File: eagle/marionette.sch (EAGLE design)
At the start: 483 parts, among them J12 IDC_RECEPTACLE_20PIN-S9172-ND, J13 CONN_HEADER_JTAG, J2 SP3T Jumper Switch, J22 ZX62D-B-5P8, J3 IDC_RECEPTACLE_2X20-S9175-ND, J5 CON_COAX_PWR_PJ-047AH-NO_MILL, J8 IDC_RECEPTACLE_2X20-S9175-ND, J9 IDC_RECEPTACLE_2X20-S9175-ND, M5002 IRFR9024NTRPBF, Q2 NFET_DUAL_DMN63D8LDW, Q3 AO3419, SW1 SW-MOM-TACTILE-B3F-1000, SW2 SW-MOM-TACTILE-B3F-1000, U1 SWITCH_74HC4066D, U10 LMV344, U11 STM32F427-STM32F427, U13 CON_HIROSE_DM3D(MICROSD), U14 USB3320, U15 SWITCH_74HC4066D, U17 LM3671, U2 FR014H5JZ, U3 MIC5305_MIC5305-3.3YD5, U4 DAC124S085CIMM, U40 MIC5305_MIC5305-3.3YD5, U41 MIC5305-MIC5305-1.8YD5, U5 MAX3051ESAESA+, U5002 TPS40200, U6 OPAMP_DUAL_MC4558CDT, U7 LMV344, U8 LMV344, U9 LMV344, X1 ABSO7

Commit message: marionette.sch incorporates Gavin's SPI4 and SPI6, I2C1/3 and GPIO rerouting, as well as the TPS63060 is in the schematic.  The schematic passes ERC.  The documentation for the TPS63060 on the board is in an ipython notebookgit add Datasheets/ Design/TPS63060_calculations.ipynb Design/ipython_files/ eagle/marionette.sch eagle/marionette.pdf eagle/marionette.lbr !
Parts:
- removed C112, C113, C114: 10u, rcl_custom:C-EUC1210
- removed C115, C144: 100p, rcl_custom:C-EU0402-B
- removed C116: 2.2n, rcl_custom:C-EU0402-B
- removed C117: np, rcl_custom:C-EU0402-B
- removed C147: 4.7u, rcl_custom:C-EU0805-B
- removed C155, C156: 100n, rcl_custom:C-EU0402-B
- removed D4: B130LB, marionette:DIODE_SCHOTTKY-_B130LB
- removed LED1, LED2, LED3, LED4, LED5, LED6: LS_Q976, LS_Q976_NR_1:LS_Q976
- removed M5002: IRFR9024NTRPBF, marionette:PFET-IRFR9024NTRPBF
- removed R22, R23, R24, R25, R26, R27: 620, rcl_custom:R-US_0402-B
- removed R5701: .050, rcl_custom:R_SENSE2512-6PAD_KELVIN_CONNECTION
- removed R69: 1.6k, rcl_custom:R-US_0402-B
- removed R71: 240k, rcl_custom:R-US_0402-B
- removed R96: 90.9k, rcl_custom:R-US_0402-B
- removed R97: 15k, rcl_custom:R-US_0402-B
- removed R98: 100k, rcl_custom:R-US_0402-B
- removed TP114, TP115, TP116, TP117, TP118, TP119, TP130, TP132: (no value), marionette:PAD+X-0.7-NO_CREAM+SILK
- removed TP201, TP61: PAD+VIA_0.6MM, marionette:PAD+VIA_0.6MM
- removed TP80: (no value), marionette:PAD+X-1.0-NO_CREAM+SILK
- removed U5002: TPS40200, marionette:TPS40200-SOIC-8_296-23923-6-ND
- added LED8: LS_Q976, LS_Q976_NR_1:LS_Q976
- added Q1: NX3020NAK, dock_v2:NFET-SOT23_NX3020NAK
- added R1, R4: 10k, rcl_custom:R-US_0402-B
- added R2: 1Meg, rcl_custom:R-US_0402-B
- added R3: 111k, rcl_custom:R-US_0402-B
- added TP29: PAD+VIA_0.25MM, dock_v2:PAD+VIA_0.25MM
- added TP74: PAD+VIA_0.635MM, dock_v2:PAD+VIA_0.635MM
- added U12: TPS63060, marionette:TPS63060
- C100, C104: value 100n -> 4.7u; device rcl_custom:C-EU0402-B -> rcl_custom:C-EUC1210; V_RATING 35V -> 25V
- C101: value 10u -> 10p; device rcl_custom:C-EUC1210 -> rcl_custom:C-EU0402-B; V_RATING 35V -> 10V
- C102: value 10u -> 100n; device rcl_custom:C-EUC1210 -> rcl_custom:C-EU0402-B; V_RATING 35V -> 25V
- C103: value 10u -> np; device rcl_custom:C-EUC1210 -> rcl_custom:C-EU1206-B; V_RATING 35V -> (none)
- C105, C106: value 10uF -> np; device rcl_custom:C-EUC1210 -> rcl_custom:C-EU1206-B; V_RATING 35V -> (none)
- C107, C108: value 10uF -> 4.7u; V_RATING 35V -> 25V
- C109: value 100n -> np; device rcl_custom:C-EU0402-B -> rcl_custom:C-EU1206-B; V_RATING 25V -> (none)
- C110: value 1n -> np; device rcl_custom:C-EU0402-B -> rcl_custom:C-EU1206-B; V_RATING 25V -> (none)
- C111: V_RATING 10V -> 25V
- C99: value 10u -> 100n; device rcl_custom:C-EUC1210 -> rcl_custom:C-EU0402-B
- L1: value SRF1260-4R7Y -> SRN3015-1R0 1uH; device marionette:INDUCTOR_COUPLED_SRF1260-4R7Y -> dock_v2:INDUCTOR_FERRITE_CORE_SRN3015-1R0
- R38: value 200k -> 10k
- R68: value 1k -> 3.3k
- TP32: value PAD+VIA_0.25MM -> (none); device marionette:PAD+VIA_0.25MM -> dock_v2:PAD+X-1.0-NO_CREAM+SILK
- TP45: value PAD+VIA_0.6MM -> (none); device marionette:PAD+VIA_0.6MM -> dock_v2:PAD+X-2.0-NOCREAM+SILK
- TP76: device marionette:PAD+X-0.7-NO_CREAM+SILK -> dock_v2:PAD+X-1.0-NO_CREAM+SILK
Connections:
- removed net I2C1_SCL: D18G4.CATHODE, J3.9, R6.1, U11G2.PB6
- removed net I2C1_SDA: J3.7, R7.1, U11G2.PB7
- removed net I2C3_SCL/ADC3_CH4: R106.1, TP111.P, TP52.TP, U11G8.PH7, U15G1.Y, U1G1.Y, U1G3.Y
- removed net I2C3_SDA/ADC3_CH8: R107.1, TP112.P, TP53.TP, U11G8.PH8, U15G2.Y, U1G2.Y, U1G4.Y
- removed net LED1_ANODE: LED1.A, R22.1, TP114.P
- removed net LED1_CATH: LED1.C, U11G7.PG9
- removed net LED2_ANODE: LED2.A, R23.1, TP115.P
- removed net LED2_CATH: LED2.C, U11G7.PG10
- removed net LED3_ANODE: LED3.A, R24.1, TP116.P
- removed net LED3_CATH: LED3.C, U11G7.PG11
- removed net LED4_ANODE: LED4.A, R25.1, TP117.P
- removed net LED4_CATH: LED4.C, U11G7.PG12
- removed net LED5_ANODE: LED5.A, R26.1, TP118.P
- removed net LED5_CATH: LED5.C, U11G7.PG13
- removed net LED6_ANODE: LED6.A, R27.1, TP119.P
- removed net LED6_CATH: LED6.C, U11G7.PG14
- removed net PG8: D16G6.CATHODE, J3.23, U11G7.PG8
- removed net SERIAL_BUS_37: J8.37, TP61.TP
- removed net SPI4_MISO: D9G3.CATHODE, J8.15, U11G5.PE13
- removed net TPS40200_CC: C100.2, C101.2, C102.2, C103.2, C99.2, D4.CATHODE, L1G2.DOT, TP32.TP
- removed net TPS40200_COMP: C117.2, R71.1, U5002.COMP
- removed net TPS40200_COMP/FB: C116.2, R71.2
- removed net TPS40200_FB: C115.1, C116.1, C117.1, R96.1, R97.2, TP132.P, U5002.FB
- removed net TPS40200_GATE_DRV: M5002.G, U5002.GDRV
- removed net TPS40200_ISNS: C110.1, R68.2, R69.2, U5002.ISNS
- removed net TPS40200_ISNS_R: R5701.PINK2, R68.1
- removed net TPS40200_RC: C144.1, R38.1, TP201.TP, U5002.RC
- removed net TPS40200_SOURCE: M5002.S, R5701.PIN2
- removed net TPS40200_SS: C109.2, TP130.P, TP45.TP, U5002.SS
- removed net TPS40200_SW: C100.1, C101.1, C102.1, C103.1, C99.1, L1G1.DOT, M5002.D, TP76.P
- removed net TPS40200_V5D/FB: C115.2, R98.1
- new net I2C1/3_SCL+ADC3_CH4: D18G4.CATHODE, J3.9, R106.1, R6.1, TP111.P, TP52.TP, U11G2.PB6, U11G8.PH7, U15G1.Y, U1G1.Y, U1G3.Y
- new net I2C1/3_SDA+ADC3_CH8: J3.7, R107.1, R7.1, TP112.P, TP53.TP, U11G2.PB7, U11G8.PH8, U15G2.Y, U1G2.Y, U1G4.Y
- new net N$5: Q1.G, R4.2, TP32.P, U12.PG
- new net N$8: LED8.A, R68.2
- new net N$9: Q1.S, R68.1
- new net PE13: J8.37, U11G5.PE13
- new net PG10: D10G4.CATHODE, J8.24, U11G7.PG10
- new net PG11: D16G6.CATHODE, J3.23, U11G7.PG11
- new net PG9: D10G5.CATHODE, J8.23, U11G7.PG9
- new net SPI6_MISO: D9G3.CATHODE, J8.15, U11G7.PG12
- new net SPI6_MOSI: D9G2.CATHODE, J8.16, U11G7.PG14
- new net SPI6_NSS: D8G6.CATHODE, J8.14, U11G7.PG8
- new net SPI6_SCK: D9G1.CATHODE, J8.13, U11G7.PG13
- new net TPS63060_EN: R1.2, TP74.TP, TP76.P, U12.EN
- new net TPS63060_FB: C101.2, R2.1, R3.2, U12.FB
- new net TPS63060_L1: L1.2, U12.L1
- new net TPS63060_L2: L1.1, U12.L2
- new net TPS63060_PS/SYNC: R38.2, TP29.TP, U12.PS/SYNC
- new net TPS63060_VAUX: C99.2, U12.VAUX
- net GND: now also C100.1, C101.1, C102.1, C103.2, C105.2, C106.2, C109.2, C110.2, C99.1, LED8.C, R3.1, U12.GND, U12.PGND; no longer C105.1, C106.1, C109.1, C112.1, C113.1, C114.1, C144.2, C147.2, C155.1, C156.1, D4.ANODE, L1G1.NOT_DOT, R97.1, U5002.GND
- net I2C2_SCL: no longer D10G4.CATHODE, J8.24
- net I2C2_SDA: no longer D10G5.CATHODE, J8.23
- net SPI4_MOSI: no longer D9G2.CATHODE, J8.16
- net SPI4_NSS: no longer D8G6.CATHODE, J8.14
- net SPI4_SCK: no longer D9G1.CATHODE, J8.13
- net V3.3D: no longer R22.2, R23.2, R24.2, R25.2, R26.2, R27.2
- net V5D: now also C100.2, C104.2, C106.1, C109.1, C110.1, R2.2, U12.VOUT; no longer C112.2, C113.2, C114.2, C147.1, L1G2.NOT_DOT, R96.2, R98.2
- net VCC: now also C102.2, C103.1, C105.1, Q1.D, R1.1, R38.1, R4.1, TP45.P, U12.VIN; no longer C104.2, C105.2, C106.2, C110.2, C155.2, C156.2, R38.2, R5701.PIN1, R5701.PINK1, R69.1, TP80.P, U5002.VCC
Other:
- note added: "(absolute max rating for TPS63060 VIN is 17V)"
- note added: "Active High (high closes switch)"
- note added: "Buck/Boost Converter Vin = 3.3V to 12V Vout = 5.0V, (up to 1.5A)"
- note added: "Coax Power Input (3.3V, 12V)"
- note added: "Pinheader Pwr Input(3.3V, 12V)"
- note removed: "0"
- note removed: "1"
- note removed: "8 pin TPS40200 shoehorns "ISNS+" and VCC (internal supply) onto same pin. Connecting low inductance power plane directly to VCC pin is best solution for current sensing and low inductance power supply to chip."
- note removed: "A"
- note removed: "Coax Power Input (3.3V, 12V, 18V)"
- note removed: "H"
- note removed: "High-Z"
- note removed: "INH"
- note removed: "L"
- note removed: "On Channel"
- note removed: "Pinheader Pwr Input(3.3V, 12V, 18V)"
- note removed: "TC7W53FK 2:1 MUX"
- note removed: "X"
- note removed: "Zeta Switching Supply Vin = 3.3V to 18V Vout = 5.0V, (up to 1.5A)"
- note removed: "fsw = 500kHz"
- moved on the sheet: C100, C101, C102, C103, C104, C105, C106, C107, C108, C109, C110, C111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

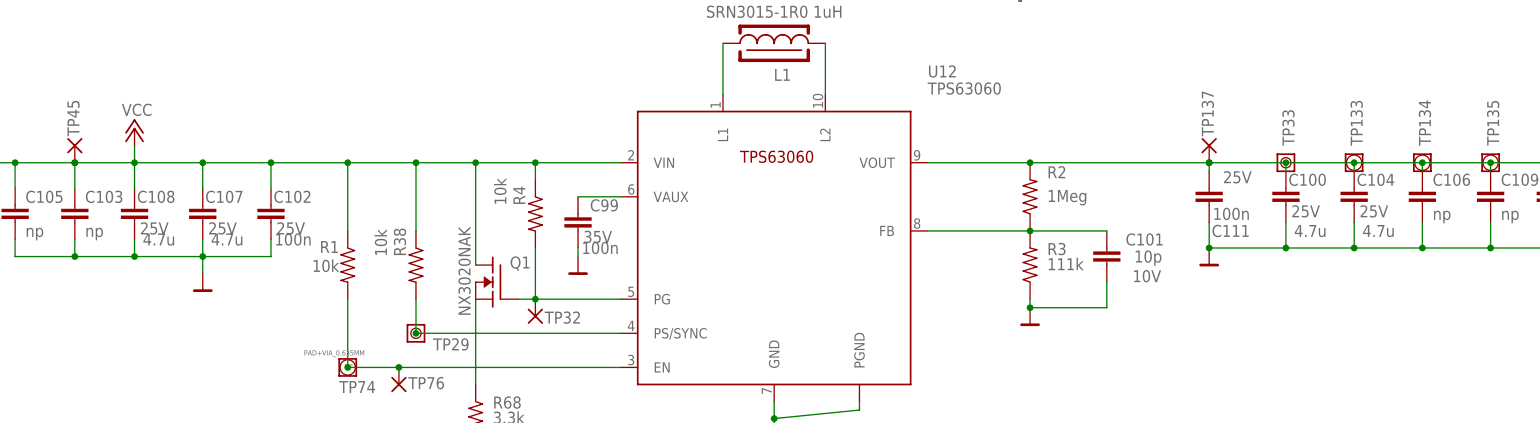
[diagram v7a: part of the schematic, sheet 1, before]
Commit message: changed some capacitor packaging on the 5V supply
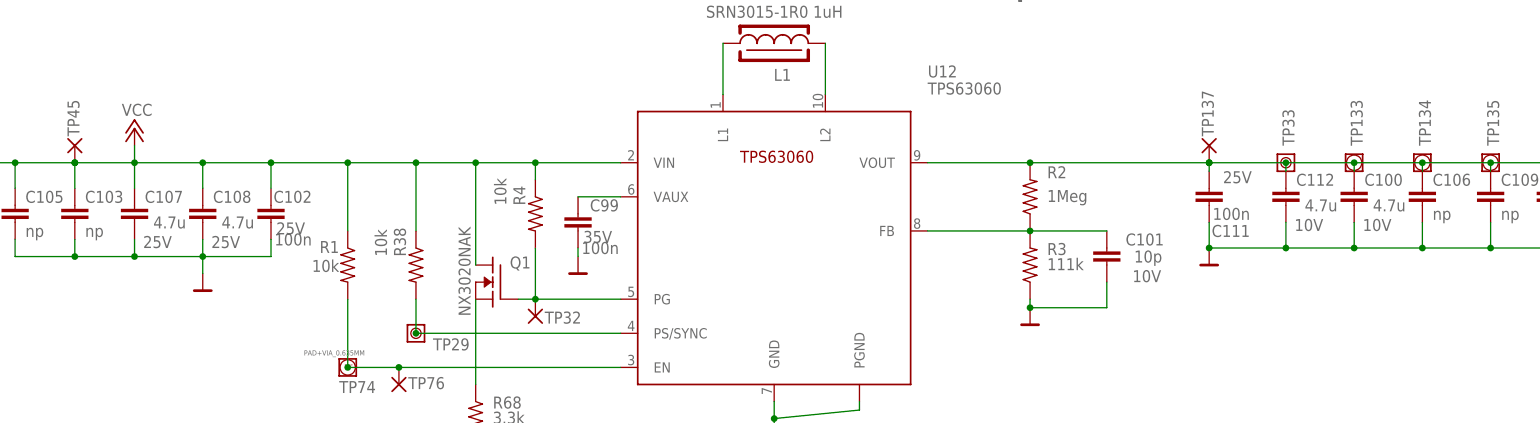
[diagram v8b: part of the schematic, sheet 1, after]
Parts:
- removed C104: 4.7u, rcl_custom:C-EUC1210
- added C112: 4.7u, rcl_custom:C-EU0805-B
- C100: device rcl_custom:C-EUC1210 -> rcl_custom:C-EU0805-B; V_RATING 25V -> 10V
- C107, C108: device rcl_custom:C-EUC1210 -> rcl_custom:C-EU0805-B
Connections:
- net N$5 renamed TPS63060_PG
- net GND: now also C100.2, C107.2, C108.2, C112.2; no longer C100.1, C104.1, C107.1, C108.1
- net V5D: now also C100.1, C112.1; no longer C100.2, C104.2
- net VCC: now also C107.1, C108.1; no longer C107.2, C108.2
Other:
- moved on the sheet: C100, C107, C108
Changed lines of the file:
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@@
 <part name="GND30" library="GROUND" deviceset="GND" device=""/>
 <part name="GND51" library="GROUND" deviceset="GND" device=""/>
-<part name="C107" library="rcl_custom" deviceset="C-EU" device="C1210" value="4.7u">
-<attribute name="V_RATING" value="25V"/>
-</part>
-<part name="C108" library="rcl_custom" deviceset="C-EU" device="C1210" value="4.7u">
-<attribute name="V_RATING" value="25V"/>
-</part>
 <part name="C111" library="rcl_custom" deviceset="C-EU" device="0402-B" value="100n">
 <attribute name="V_RATING" value="25V"/>
@@
 <part name="TP76" library="dock_v2" deviceset="PAD+X" device="-1.0-NO_CREAM+SILK"/>
 <part name="L1" library="dock_v2" deviceset="INDUCTOR_FERRITE_CORE" device="_SRN3015-1R0" value="SRN3015-1R0 1uH"/>
-<part name="C100" library="rcl_custom" deviceset="C-EU" device="C1210" value="4.7u">
-<attribute name="V_RATING" value="25V"/>
-</part>
 <part name="C102" library="rcl_custom" deviceset="C-EU" device="0402-B" value="100n">
 <attribute name="V_RATING" value="25V"/>
 </part>
 <part name="C103" library="rcl_custom" deviceset="C-EU" device="1206-B" value="np"/>
-<part name="C104" library="rcl_custom" deviceset="C-EU" device="C1210" value="4.7u">
-<attribute name="V_RATING" value="25V"/>
-</part>
 <part name="C105" library="rcl_custom" deviceset="C-EU" device="1206-B" value="np"/>
 <part name="C106" library="rcl_custom" deviceset="C-EU" device="1206-B" value="np"/>
@@
 <part name="R68" library="rcl_custom" deviceset="R-US_" device="0402-B" value="3.3k"/>
 <part name="GND103" library="supply" deviceset="GND" device=""/>
+<part name="C107" library="rcl_custom" deviceset="C-EU" device="0805-B" value="4.7u">
+<attribute name="V_RATING" value="25V"/>
+</part>
+<part name="C108" library="rcl_custom" deviceset="C-EU" device="0805-B" value="4.7u">
+<attribute name="V_RATING" value="25V"/>
+</part>
+<part name="C112" library="rcl_custom" deviceset="C-EU" device="0805-B" value="4.7u">
+<attribute name="V_RATING" value="10V"/>
+</part>
+<part name="C100" library="rcl_custom" deviceset="C-EU" device="0805-B" value="4.7u">
+<attribute name="V_RATING" value="10V"/>
+</part>
 </parts>
 <sheets>
@@
 <instance part="GND30" gate="1" x="60.96" y="457.2"/>
 <instance part="GND51" gate="1" x="60.96" y="411.48"/>
-<instance part="C107" gate="CE" x="313.69" y="463.55" smashed="yes" rot="R180">
-<attribute name="V_RATING" x="318.77" y="463.55" size="1.778" layer="96" rot="R180"/>
-<attribute name="NAME" x="319.786" y="468.249" size="1.778" layer="95" rot="R180"/>
-<attribute name="VALUE" x="319.786" y="461.899" size="1.778" layer="96" rot="R180"/>
-</instance>
-<instance part="C108" gate="CE" x="303.53" y="463.55" smashed="yes" rot="R180">
-<attribute name="V_RATING" x="308.61" y="463.55" size="1.778" layer="96" rot="R180"/>
-<attribute name="NAME" x="309.626" y="468.249" size="1.778" layer="95" rot="R180"/>
-<attribute name="VALUE" x="309.626" y="461.899" size="1.778" layer="96" rot="R180"/>
-</instance>
 <instance part="C111" gate="CE" x="463.55" y="466.09" smashed="yes" rot="R180">
 <attribute name="V_RATING" x="469.9" y="471.17" size="1.778" layer="96" rot="R180"/>
@@
 <attribute name="VALUE" x="388.62" y="494.03" size="1.778" layer="96" ratio="20"/>
 </instance>
-<instance part="C100" gate="CE" x="474.98" y="466.09" smashed="yes" rot="R180">
-<attribute name="V_RATING" x="480.06" y="466.09" size="1.778" layer="96" rot="R180"/>
-<attribute name="NAME" x="481.076" y="470.789" size="1.778" layer="95" rot="R180"/>
-<attribute name="VALUE" x="481.076" y="463.169" size="1.778" layer="96" rot="R180"/>
-</instance>
 <instance part="C102" gate="CE" x="323.85" y="463.55" smashed="yes" rot="R180">
 <attribute name="V_RATING" x="328.93" y="463.55" size="1.778" layer="96" rot="R180"/>
@@
 </instance>
 <instance part="C103" gate="CE" x="294.64" y="466.09"/>
-<instance part="C104" gate="CE" x="485.14" y="466.09" smashed="yes" rot="R180">
-<attribute name="V_RATING" x="490.22" y="466.09" size="1.778" layer="96" rot="R180"/>
-<attribute name="NAME" x="491.236" y="470.789" size="1.778" layer="95" rot="R180"/>
-<attribute name="VALUE" x="491.236" y="463.169" size="1.778" layer="96" rot="R180"/>
-</instance>
 <instance part="C105" gate="CE" x="285.75" y="466.09"/>
 <instance part="C106" gate="CE" x="495.3" y="468.63"/>
@@
 </instance>
 <instance part="GND103" gate="G1" x="354.33" y="416.56"/>
+<instance part="C107" gate="CE" x="303.53" y="466.09" smashed="yes">
+<attribute name="V_RATING" x="304.8" y="459.74" size="1.778" layer="96"/>
+<attribute name="NAME" x="305.054" y="466.471" size="1.778" layer="95"/>
+<attribute name="VALUE" x="306.324" y="462.661" size="1.778" layer="96"/>
+</instance>
+<instance part="C108" gate="CE" x="313.69" y="466.09" smashed="yes">
+<attribute name="V_RATING" x="314.96" y="459.74" size="1.778" layer="96"/>
+<attribute name="NAME" x="315.214" y="466.471" size="1.778" layer="95"/>
+<attribute name="VALUE" x="316.484" y="462.661" size="1.778" layer="96"/>
+</instance>
+<instance part="C112" gate="CE" x="474.98" y="468.63" smashed="yes">
+<attribute name="V_RATING" x="476.25" y="462.28" size="1.778" layer="96"/>
+<attribute name="NAME" x="476.504" y="469.011" size="1.778" layer="95"/>
+<attribute name="VALUE" x="477.774" y="465.201" size="1.778" layer="96"/>
+</instance>
+<instance part="C100" gate="CE" x="485.14" y="468.63" smashed="yes">
+<attribute name="V_RATING" x="486.41" y="462.28" size="1.778" layer="96"/>
+<attribute name="NAME" x="486.664" y="469.011" size="1.778" layer="95"/>
+<attribute name="VALUE" x="487.934" y="465.201" size="1.778" layer="96"/>
+</instance>
 </instances>
 <busses>
@@
 <wire x1="463.55" y1="459.74" x2="463.55" y2="463.55" width="0.1524" layer="91"/>
 <pinref part="GND5015" gate="G1" pin="GND"/>
-<pinref part="C100" gate="CE" pin="1"/>
 <wire x1="463.55" y1="459.74" x2="474.98" y2="459.74" width="0.1524" layer="91"/>
 <wire x1="474.98" y1="459.74" x2="474.98" y2="463.55" width="0.1524" layer="91"/>
 <junction x="463.55" y="459.74"/>
-<pinref part="C104" gate="CE" pin="1"/>
 <wire x1="474.98" y1="459.74" x2="485.14" y2="459.74" width="0.1524" layer="91"/>
 <wire x1="485.14" y1="459.74" x2="485.14" y2="463.55" width="0.1524" layer="91"/>
@@
 <wire x1="514.35" y1="459.74" x2="514.35" y2="463.55" width="0.1524" layer="91"/>
 <junction x="505.46" y="459.74"/>
+<pinref part="C112" gate="CE" pin="2"/>
+<pinref part="C100" gate="CE" pin="2"/>
 </segment>
 <segment>
@@
 <pinref part="GND5006" gate="G1" pin="GND"/>
 <wire x1="313.69" y1="455.93" x2="313.69" y2="458.47" width="0.1524" layer="91"/>
-<pinref part="C107" gate="CE" pin="1"/>
 <wire x1="313.69" y1="458.47" x2="313.69" y2="461.01" width="0.1524" layer="91"/>
-<pinref part="C108" gate="CE" pin="1"/>
 <wire x1="313.69" y1="458.47" x2="303.53" y2="458.47" width="0.1524" layer="91"/>
 <wire x1="303.53" y1="458.47" x2="303.53" y2="461.01" width="0.1524" layer="91"/>
@@
 <wire x1="285.75" y1="458.47" x2="285.75" y2="461.01" width="0.1524" layer="91"/>
 <junction x="294.64" y="458.47"/>
+<pinref part="C107" gate="CE" pin="2"/>
+<pinref part="C108" gate="CE" pin="2"/>
 </segment>
 <segment>
@@
 <segment>
 <pinref part="V1" gate="G1" pin="VCC"/>
-<pinref part="C108" gate="CE" pin="2"/>
 <wire x1="303.53" y1="468.63" x2="303.53" y2="472.44" width="0.1524" layer="91"/>
 <wire x1="303.53" y1="472.44" x2="303.53" y2="474.98" width="0.1524" layer="91"/>
@@
 <wire x1="294.64" y1="472.44" x2="303.53" y2="472.44" width="0.3048" layer="91"/>
 <wire x1="303.53" y1="472.44" x2="313.69" y2="472.44" width="0.3048" layer="91"/>
-<pinref part="C107" gate="CE" pin="2"/>
 <wire x1="313.69" y1="468.63" x2="313.69" y2="472.44" width="0.1524" layer="91"/>
 <junction x="313.69" y="472.44"/>
@@
 <wire x1="354.33" y1="457.2" x2="354.33" y2="472.44" width="0.1524" layer="91"/>
 <junction x="354.33" y="472.44"/>
+<pinref part="C107" gate="CE" pin="1"/>
+<pinref part="C108" gate="CE" pin="1"/>
 </segment>
 </net>
@@
 <junction x="436.88" y="472.44"/>
 <junction x="463.55" y="472.44"/>
-<pinref part="C100" gate="CE" pin="2"/>
-<pinref part="C104" gate="CE" pin="2"/>
 <pinref part="C106" gate="CE" pin="1"/>
 <pinref part="C109" gate="CE" pin="1"/>
@@
 <wire x1="514.35" y1="471.17" x2="514.35" y2="472.44" width="0.1524" layer="91"/>
 <junction x="514.35" y="472.44"/>
+<pinref part="C112" gate="CE" pin="1"/>
+<pinref part="C100" gate="CE" pin="1"/>
 </segment>
 <segment>
@@
 </segment>
 </net>
-<net name="N$5" class="0">
+<net name="TPS63060_PG" class="0">
 <segment>
 <pinref part="R4" gate="R" pin="2"/>
